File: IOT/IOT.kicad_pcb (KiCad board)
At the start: 2 copper layers, 19 parts, among them J1 OLED, J2 I2C_DEV, J3 UART_DEV

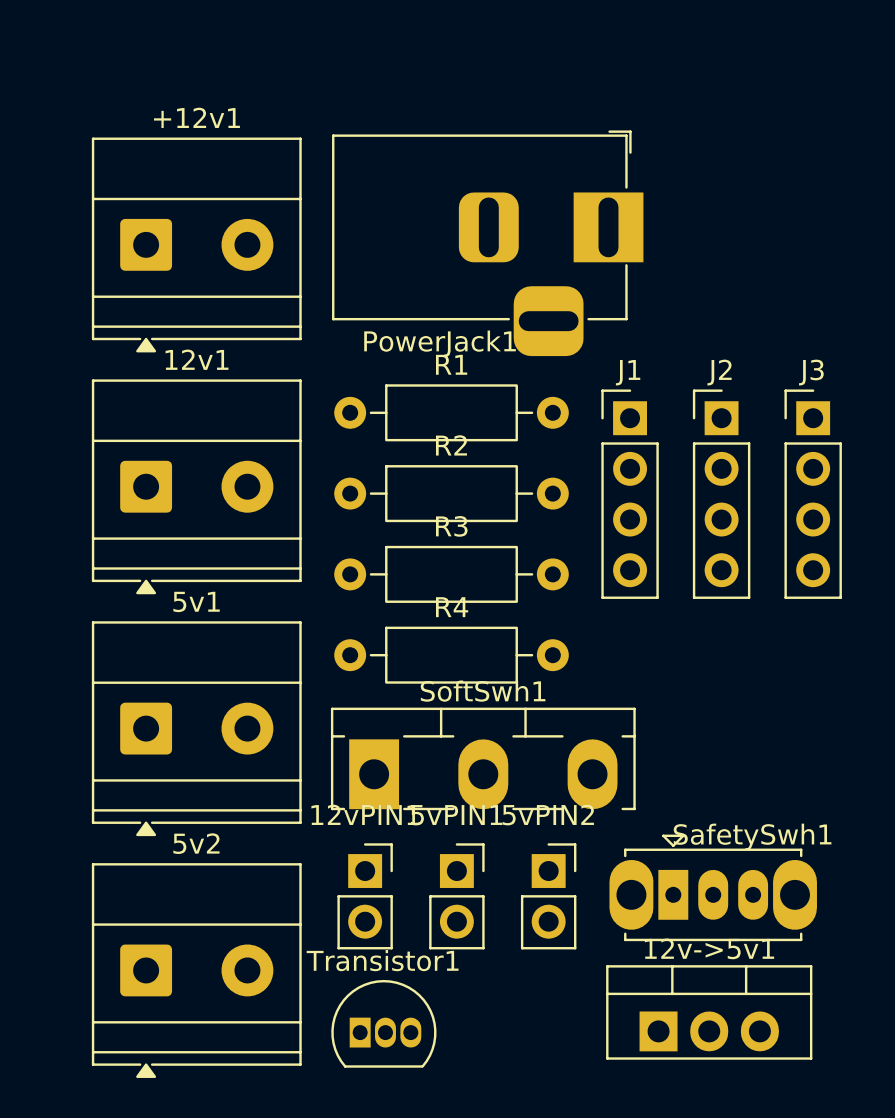
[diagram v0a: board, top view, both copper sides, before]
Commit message: Convert Core to submodule and update project state
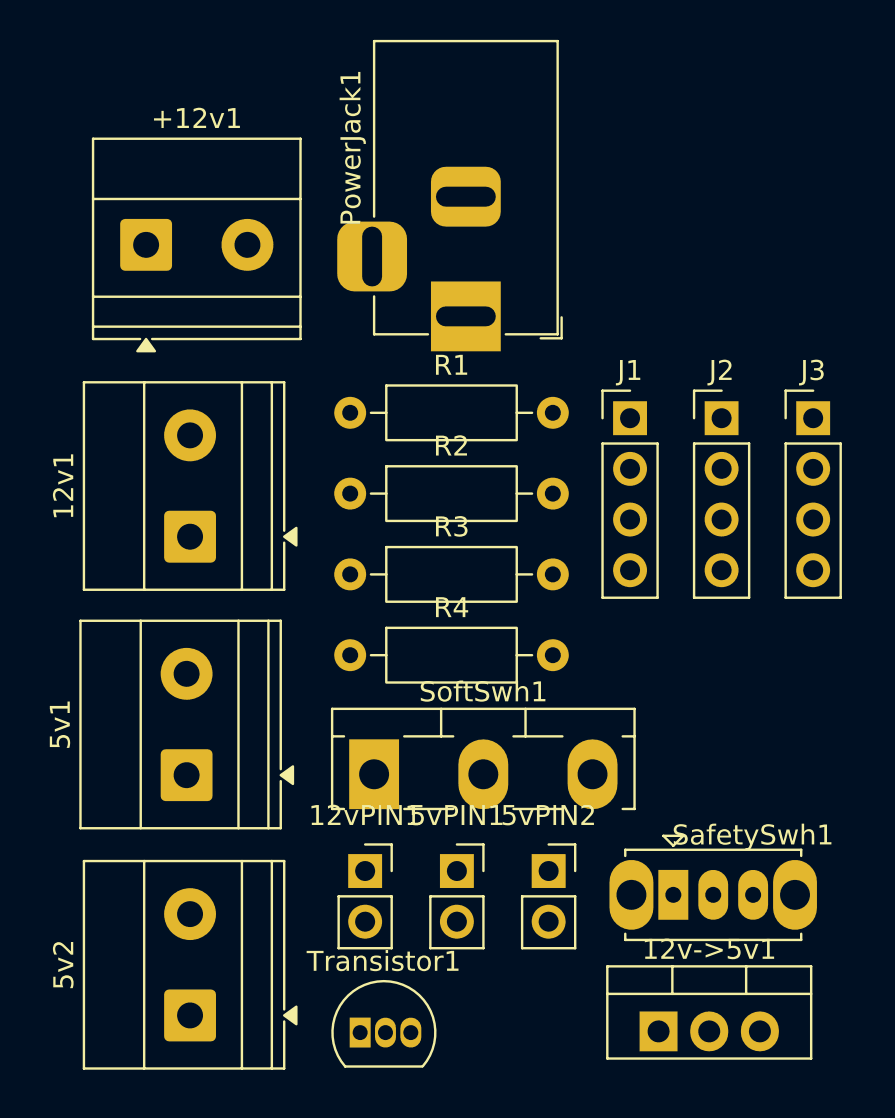
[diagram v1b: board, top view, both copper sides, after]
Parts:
- moved PowerJack1 8.43 mm to (196.0, 49.5), turned to -90 degrees
- moved 12v1 3.34 mm to (182.2, 60.5), turned to 90 degrees
- moved 5v2 3.15 mm to (182.2, 84.5), turned to 90 degrees
- moved 5v1 3.09 mm to (182.0, 72.5), turned to 90 degrees
